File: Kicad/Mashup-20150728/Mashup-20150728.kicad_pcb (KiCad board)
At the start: 2 copper layers, 99.1 x 88.9 mm, 132 parts, among them P1 TST, P10 SPADE_187, P2 CONN_4, P3 CONN_4, P4 CONN2X3MOLEX, P4 CONN_4, P4 CONN_6, P4 SPADE_187, P5 CONN_4, P5 CONN_4X2, P5 CONN_8, P6 CONN_2, P6 CONN_4, P6 CONN_4X2, P6 CONN_8, P7 CONN_4, P7 CONN_8, Q1 MOSFET_N, Q2 MOSFET_N, Q3 MOSFET_N, Q4 MOSFET_N, Q5 MOSFET_N, Q6 MOSFET_N, Q7 MOSFET_N, Q8 MOSFET_N

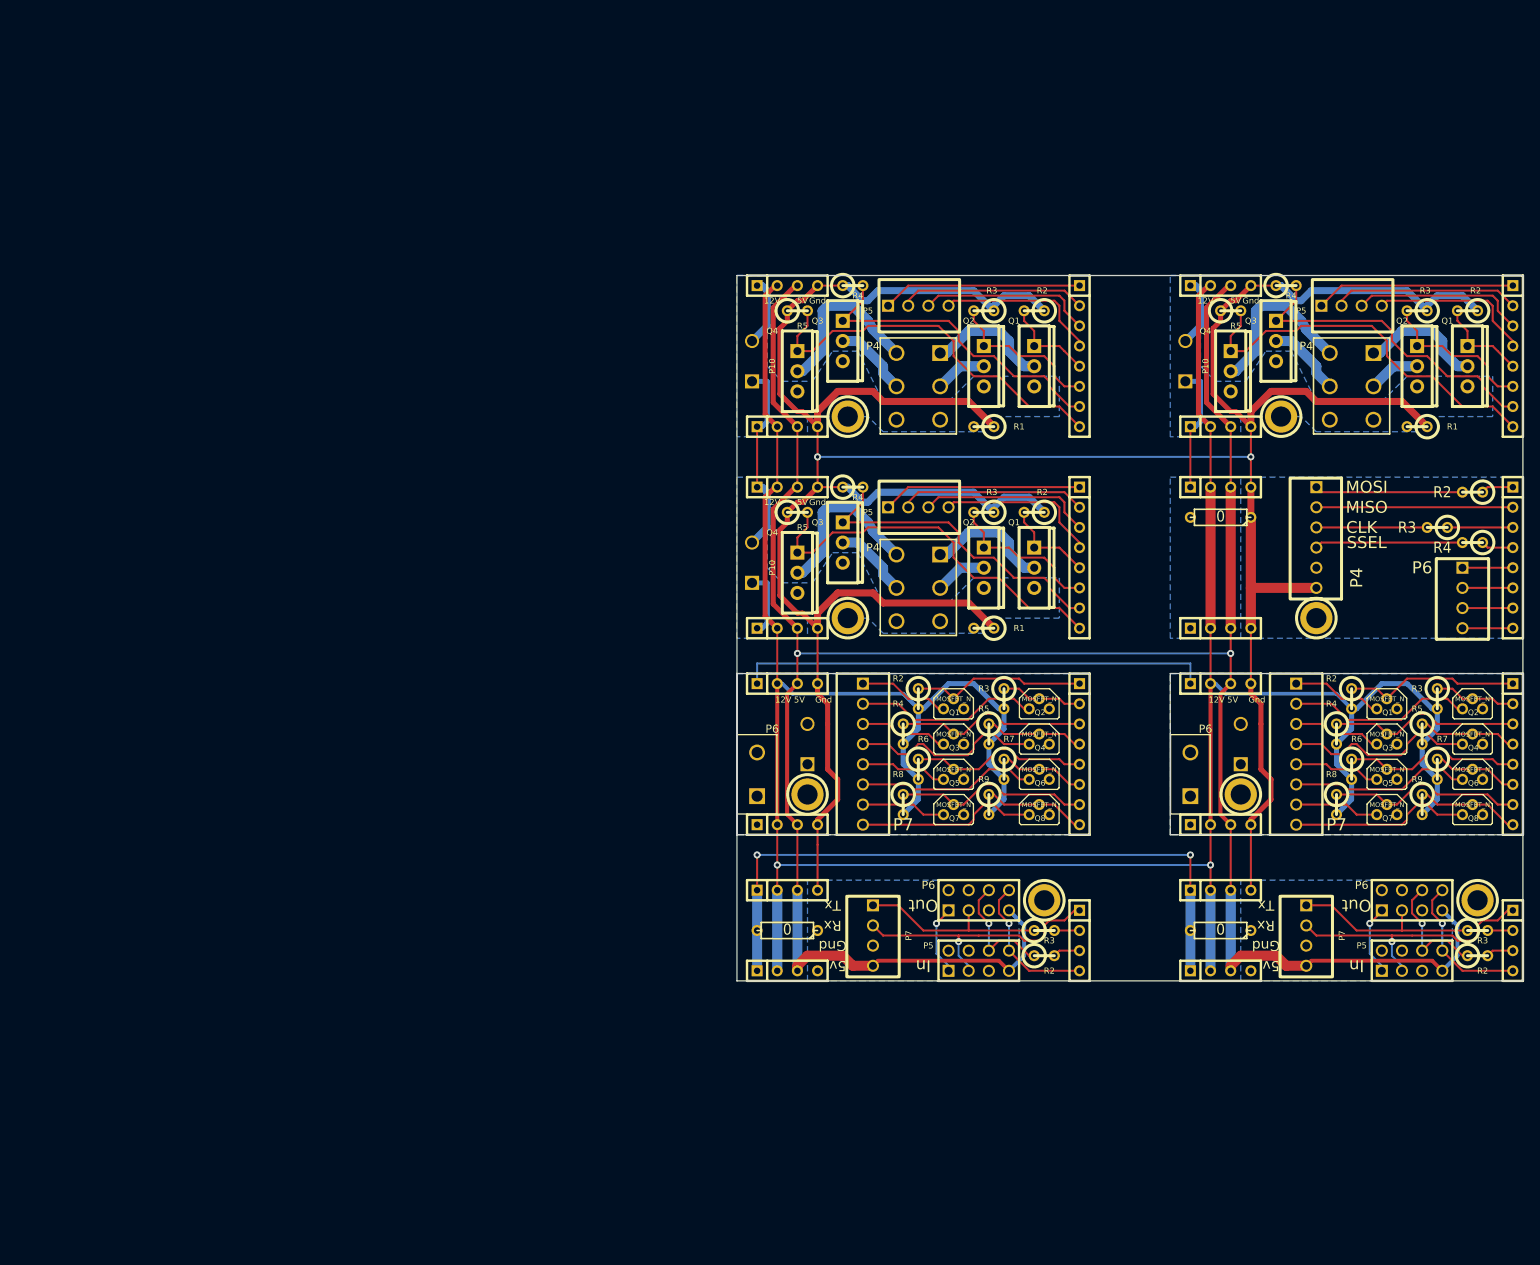
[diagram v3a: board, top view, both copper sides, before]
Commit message: Changed size of PCB sheets to 8.5" x 11".  Added name/rev/board name to PCB sheets.
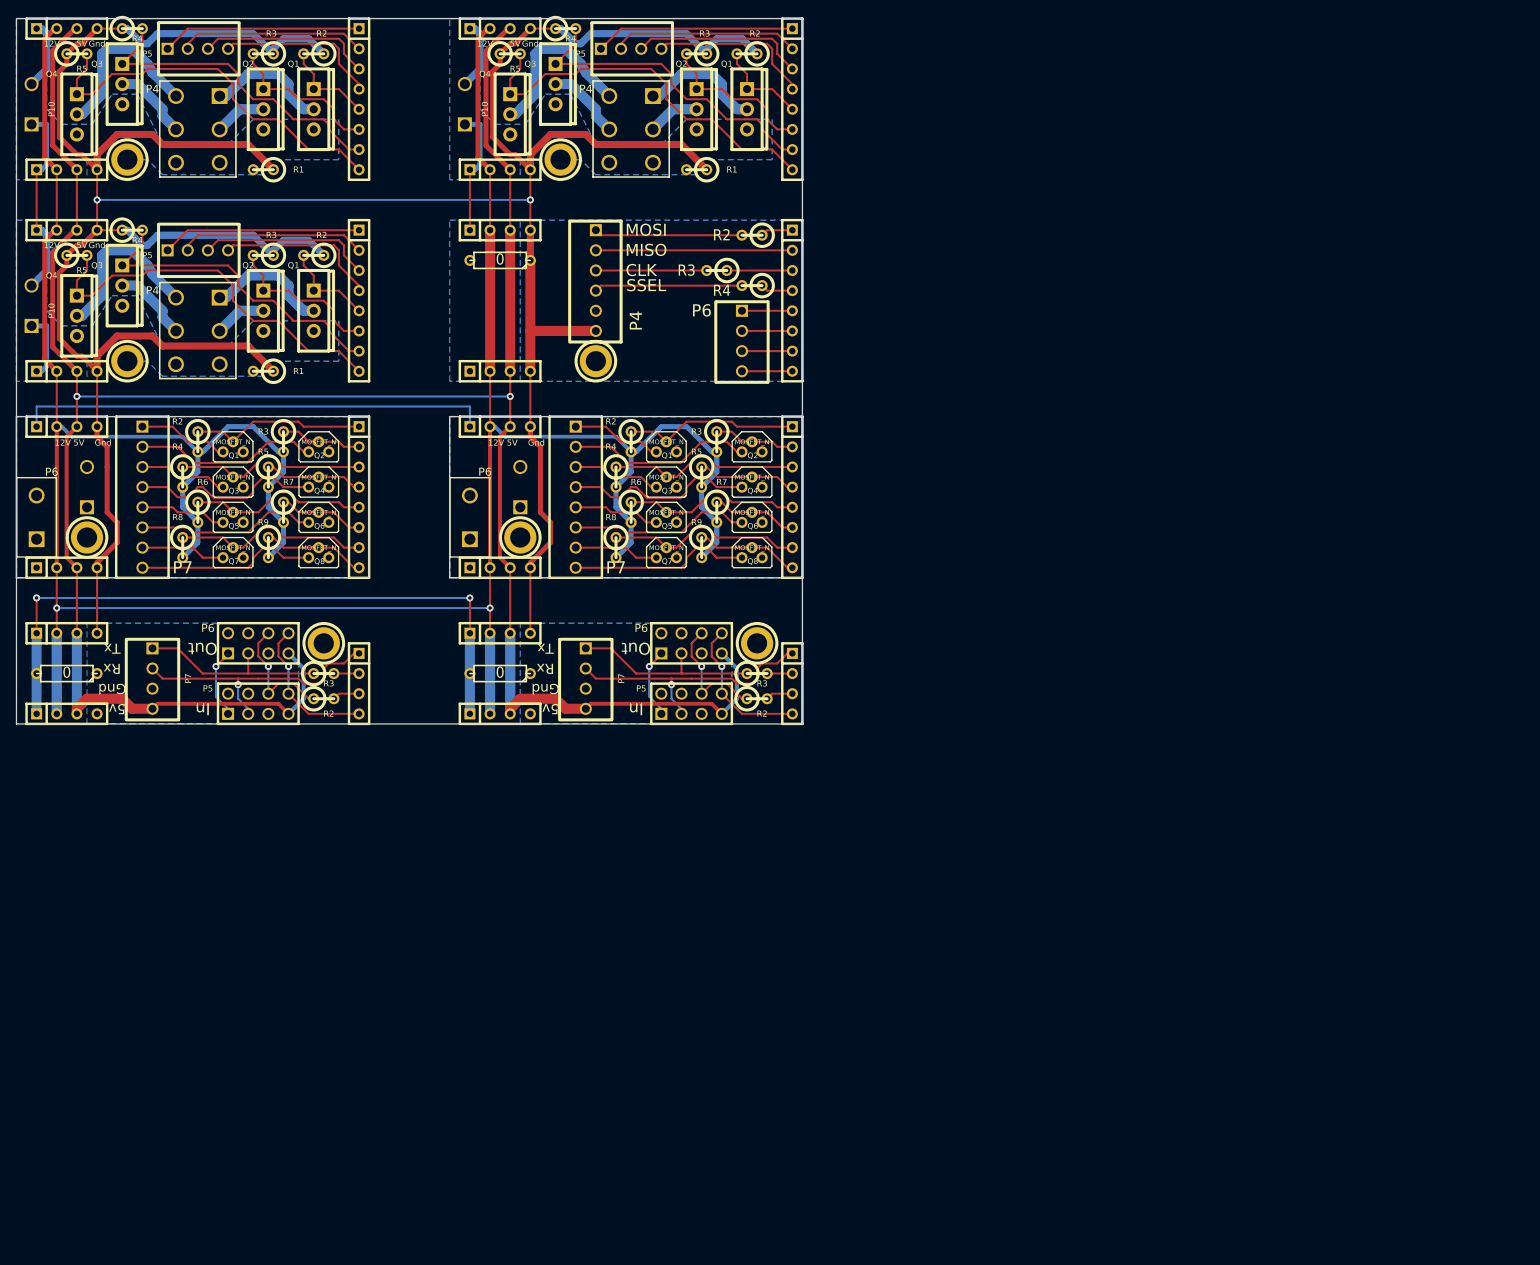
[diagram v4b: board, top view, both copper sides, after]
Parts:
- removed the P1 at (139.7, 106.7)
- removed the P1 at (194.3, 81.3)
- removed the P1 at (139.7, 81.3)
- removed the P1 at (219.1, 142.2)
- removed the P1 at (164.5, 142.2)
- removed the P1 at (134.6, 128.9)
- removed the P1 at (189.2, 128.9)
- removed the P10 at (182.2, 74.3)
- removed the P10 at (127.6, 99.7)
- removed the P10 at (127.6, 74.3)
- removed the P2 at (186.7, 64.8)
- removed the P2 at (132.1, 90.2)
- removed the P2 at (132.1, 64.8)
- removed the P2 at (186.7, 151.1)
- removed the P2 at (132.1, 151.1)
- removed the P2 at (132.1, 114.9)
- removed the P2 at (186.7, 114.9)
- removed the P3 at (186.7, 82.5)
- removed the P3 at (132.1, 108.0)
- removed the P3 at (132.1, 82.5)
- removed the P3 at (186.7, 141.0)
- removed the P3 at (132.1, 141.0)
- removed the P3 at (132.1, 132.7)
- removed the P3 at (186.7, 132.7)
- removed the P4 at (203.2, 77.5)
- removed the P4 at (148.6, 102.9)
- removed the P4 at (148.6, 77.5)
- removed the P4 at (223.5, 147.3)
- removed the P4 at (168.9, 147.3)
- removed the P4 at (134.6, 122.6)
- removed the P4 at (189.2, 122.6)
- removed the P5 at (203.2, 67.3)
- removed the P5 at (148.6, 92.7)
- removed the P5 at (148.6, 67.3)
- removed the P5 at (210.8, 149.9)
- removed the P5 at (156.2, 149.9)
- removed the P5 at (168.9, 123.8)
- removed the P5 at (223.5, 123.8)
- removed the P6 at (223.5, 73.7)
- removed the P6 at (168.9, 99.1)
- removed the P6 at (168.9, 73.7)
- removed the P6 at (210.8, 142.2)
- removed the P6 at (156.2, 142.2)
- removed the P6 at (128.3, 126.4)
- removed the P6 at (182.9, 126.4)
- removed the P7 at (197.5, 146.7)
- removed the P7 at (142.9, 146.7)
- removed the P7 at (141.6, 123.8)
- removed the P7 at (196.2, 123.8)
- removed the Q1 at (217.8, 74.9)
- removed the Q1 at (163.2, 100.3)
- removed the Q1 at (163.2, 74.9)
- removed the Q1 at (153.0, 117.5)
- removed the Q1 at (207.6, 117.5)
- removed the Q2 at (211.5, 74.9)
- removed the Q2 at (156.8, 100.3)
- removed the Q2 at (156.8, 74.9)
- removed the Q2 at (163.8, 117.5)
- removed the Q2 at (218.4, 117.5)
- removed the Q3 at (193.7, 71.8)
- removed the Q3 at (139.1, 97.2)
- removed the Q3 at (139.1, 71.8)
- removed the Q3 at (153.0, 121.9)
- removed the Q3 at (207.6, 121.9)
- removed the Q4 at (188.0, 75.6)
- removed the Q4 at (133.3, 101.0)
- removed the Q4 at (133.3, 75.6)
- removed the Q4 at (163.8, 121.9)
- removed the Q4 at (218.4, 121.9)
- removed the Q5 at (153.0, 126.4)
- removed the Q5 at (207.6, 126.4)
- removed the Q6 at (163.8, 126.4)
- removed the Q6 at (218.4, 126.4)
- removed the Q7 at (153.0, 130.8)
- removed the Q7 at (207.6, 130.8)
- removed the Q8 at (163.8, 130.8)
- removed the Q8 at (218.4, 130.8)
- removed the R1 at (211.5, 82.5)
- removed the R1 at (156.8, 108.0)
- removed the R1 at (156.8, 82.5)
- removed the R1 at (186.7, 146.1)
- removed the R1 at (132.1, 146.1)
- removed the R2 at (217.8, 67.9)
- removed the R2 at (163.2, 93.3)
- removed the R2 at (163.2, 67.9)
- removed the R2 at (219.1, 149.2)
- removed the R2 at (164.5, 149.2)
- removed the R2 at (148.6, 116.8)
- removed the R2 at (203.2, 116.8)
- removed the R3 at (211.5, 67.9)
- removed the R3 at (156.8, 93.3)
- removed the R3 at (156.8, 67.9)
- removed the R3 at (219.1, 146.1)
- removed the R3 at (164.5, 146.1)
- removed the R3 at (159.4, 116.8)
- removed the R3 at (214.0, 116.8)
- removed the R4 at (194.9, 64.8)
- removed the R4 at (140.3, 90.2)
- removed the R4 at (140.3, 64.8)
- removed the R4 at (146.7, 121.3)
- removed the R4 at (201.3, 121.3)
- removed the R5 at (188.0, 67.9)
- removed the R5 at (133.3, 93.3)
- removed the R5 at (133.3, 67.9)
- removed the R5 at (157.5, 121.3)
- removed the R5 at (212.1, 121.3)
- removed the R6 at (148.6, 125.7)
- removed the R6 at (203.2, 125.7)
- removed the R7 at (159.4, 125.7)
- removed the R7 at (214.0, 125.7)
- removed the R8 at (146.7, 130.2)
- removed the R8 at (201.3, 130.2)
- removed the R9 at (157.5, 130.2)
- removed the R9 at (212.1, 130.2)
- removed the VAL at (138.4, 122.6)
- removed the VAL at (193.0, 122.6)
- added P1: TST, 00_mtg_hole-2-56, F.Cu at (48.9, 74.3)
- added P1: TST, 00_mtg_hole-2-56, F.Cu at (103.5, 48.9)
- added P1: TST, 00_mtg_hole-2-56, F.Cu at (48.9, 48.9)
- added P1: TST, 00_mtg_hole-2-56, F.Cu at (128.3, 109.9)
- added P1: TST, 00_mtg_hole-2-56, F.Cu at (73.7, 109.9)
- added P1: TST, 00_mtg_hole-2-56, F.Cu at (43.8, 96.5)
- added P1: TST, 00_mtg_hole-2-56, F.Cu at (98.4, 96.5)
- added P10: SPADE_187, 00_th1x2x200, F.Cu at (91.4, 41.9)
- added P10: SPADE_187, 00_th1x2x200, F.Cu at (36.8, 67.3)
- added P10: SPADE_187, 00_th1x2x200, F.Cu at (36.8, 41.9)
- added P2: CONN_4, SIL-4, F.Cu at (95.9, 32.4)
- added P2: CONN_4, SIL-4, F.Cu at (41.3, 57.8)
- added P2: CONN_4, SIL-4, F.Cu at (41.3, 32.4)
- added P2: CONN_4, SIL-4, F.Cu at (95.9, 118.7)
- added P2: CONN_4, SIL-4, F.Cu at (41.3, 118.7)
- added P2: CONN_4, SIL-4, F.Cu at (41.3, 82.5)
- added P2: CONN_4, SIL-4, F.Cu at (95.9, 82.5)
- added P3: CONN_4, SIL-4, F.Cu at (95.9, 50.2)
- added P3: CONN_4, SIL-4, F.Cu at (41.3, 75.6)
- added P3: CONN_4, SIL-4, F.Cu at (41.3, 50.2)
- added P3: CONN_4, SIL-4, F.Cu at (95.9, 108.6)
- added P3: CONN_4, SIL-4, F.Cu at (41.3, 108.6)
- added P3: CONN_4, SIL-4, F.Cu at (41.3, 100.3)
- added P3: CONN_4, SIL-4, F.Cu at (95.9, 100.3)
- added P4: CONN2X3MOLEX, 00_th2x3x4.2mm_nopeg, F.Cu at (112.4, 45.1)
- added P4: CONN2X3MOLEX, 00_th2x3x4.2mm_nopeg, F.Cu at (57.8, 70.5)
- added P4: CONN2X3MOLEX, 00_th2x3x4.2mm_nopeg, F.Cu at (57.8, 45.1)
- added P4: CONN_4, SIL-4, F.Cu at (132.7, 114.9)
- added P4: CONN_4, SIL-4, F.Cu at (78.1, 114.9)
- added P4: SPADE_187, 00_th1x2x200, F.Cu at (43.8, 90.2)
- added P4: SPADE_187, 00_th1x2x200, F.Cu at (98.4, 90.2)
- added P5: CONN_4, 00_th1x4x100-lock, F.Cu at (112.4, 34.9)
- added P5: CONN_4, 00_th1x4x100-lock, F.Cu at (57.8, 60.3)
- added P5: CONN_4, 00_th1x4x100-lock, F.Cu at (57.8, 34.9)
- added P5: CONN_4X2, pin_array_4x2, F.Cu at (120.0, 117.5)
- added P5: CONN_4X2, pin_array_4x2, F.Cu at (65.4, 117.5)
- added P5: CONN_8, SIL-8, F.Cu at (78.1, 91.4)
- added P5: CONN_8, SIL-8, F.Cu at (132.7, 91.4)
- added P6: CONN_8, SIL-8, F.Cu at (132.7, 41.3)
- added P6: CONN_8, SIL-8, F.Cu at (78.1, 66.7)
- added P6: CONN_8, SIL-8, F.Cu at (78.1, 41.3)
- added P6: CONN_4X2, pin_array_4x2, F.Cu at (120.0, 109.9)
- added P6: CONN_4X2, pin_array_4x2, F.Cu at (65.4, 109.9)
- added P6: CONN_2, 00_th1x2x4.2mm_nopeg, F.Cu at (37.5, 94.0)
- added P6: CONN_2, 00_th1x2x4.2mm_nopeg, F.Cu at (92.1, 94.0)
- added P7: CONN_4, 00_th1x4x100-lock, F.Cu at (106.7, 114.3)
- added P7: CONN_4, 00_th1x4x100-lock, F.Cu at (52.1, 114.3)
- added P7: CONN_8, 00_th1x8x100-lock, F.Cu at (50.8, 91.4)
- added P7: CONN_8, 00_th1x8x100-lock, F.Cu at (105.4, 91.4)
- added Q1: MOSFET_N, 00_to220_vert_gds, F.Cu at (127.0, 42.5)
- added Q1: MOSFET_N, 00_to220_vert_gds, F.Cu at (72.4, 67.9)
- added Q1: MOSFET_N, 00_to220_vert_gds, F.Cu at (72.4, 42.5)
- added Q1: MOSFET_N, 00_to92_sgd, F.Cu at (62.2, 85.1)
- added Q1: MOSFET_N, 00_to92_sgd, F.Cu at (116.8, 85.1)
- added Q2: MOSFET_N, 00_to220_vert_gds, F.Cu at (120.7, 42.5)
- added Q2: MOSFET_N, 00_to220_vert_gds, F.Cu at (66.0, 67.9)
- added Q2: MOSFET_N, 00_to220_vert_gds, F.Cu at (66.0, 42.5)
- added Q2: MOSFET_N, 00_to92_sgd, F.Cu at (73.0, 85.1)
- added Q2: MOSFET_N, 00_to92_sgd, F.Cu at (127.6, 85.1)
- added Q3: MOSFET_N, 00_to220_vert_gds, F.Cu at (102.9, 39.4)
- added Q3: MOSFET_N, 00_to220_vert_gds, F.Cu at (48.3, 64.8)
- added Q3: MOSFET_N, 00_to220_vert_gds, F.Cu at (48.3, 39.4)
- added Q3: MOSFET_N, 00_to92_sgd, F.Cu at (62.2, 89.5)
- added Q3: MOSFET_N, 00_to92_sgd, F.Cu at (116.8, 89.5)
- added Q4: MOSFET_N, 00_to220_vert_gds, F.Cu at (97.2, 43.2)
- added Q4: MOSFET_N, 00_to220_vert_gds, F.Cu at (42.5, 68.6)
- added Q4: MOSFET_N, 00_to220_vert_gds, F.Cu at (42.5, 43.2)
- added Q4: MOSFET_N, 00_to92_sgd, F.Cu at (73.0, 89.5)
- added Q4: MOSFET_N, 00_to92_sgd, F.Cu at (127.6, 89.5)
- added Q5: MOSFET_N, 00_to92_sgd, F.Cu at (62.2, 94.0)
- added Q5: MOSFET_N, 00_to92_sgd, F.Cu at (116.8, 94.0)
- added Q6: MOSFET_N, 00_to92_sgd, F.Cu at (73.0, 94.0)
- added Q6: MOSFET_N, 00_to92_sgd, F.Cu at (127.6, 94.0)
- added Q7: MOSFET_N, 00_to92_sgd, F.Cu at (62.2, 98.4)
- added Q7: MOSFET_N, 00_to92_sgd, F.Cu at (116.8, 98.4)
- added Q8: MOSFET_N, 00_to92_sgd, F.Cu at (73.0, 98.4)
- added Q8: MOSFET_N, 00_to92_sgd, F.Cu at (127.6, 98.4)
- added R1: 100K, R1, F.Cu at (120.7, 50.2)
- added R1: 100K, R1, F.Cu at (66.0, 75.6)
- added R1: 100K, R1, F.Cu at (66.0, 50.2)
- added R1: 0, R3, F.Cu at (95.9, 113.7)
- added R1: 0, R3, F.Cu at (41.3, 113.7)
- added R2: 100K, R1, F.Cu at (127.0, 35.6)
- added R2: 100K, R1, F.Cu at (72.4, 61.0)
- added R2: 100K, R1, F.Cu at (72.4, 35.6)
- added R2: 480, R1, F.Cu at (128.3, 116.8)
- added R2: 480, R1, F.Cu at (73.7, 116.8)
- added R2: 10K, R1, F.Cu at (57.8, 84.5)
- added R2: 10K, R1, F.Cu at (112.4, 84.5)
- added R3: 100K, R1, F.Cu at (120.7, 35.6)
- added R3: 100K, R1, F.Cu at (66.0, 61.0)
- added R3: 100K, R1, F.Cu at (66.0, 35.6)
- added R3: 480, R1, F.Cu at (128.3, 113.7)
- added R3: 480, R1, F.Cu at (73.7, 113.7)
- added R3: 10K, R1, F.Cu at (68.6, 84.5)
- added R3: 10K, R1, F.Cu at (123.2, 84.5)
- added R4: 100K, R1, F.Cu at (104.1, 32.4)
- added R4: 100K, R1, F.Cu at (49.5, 57.8)
- added R4: 100K, R1, F.Cu at (49.5, 32.4)
- added R4: 10K, R1, F.Cu at (55.9, 88.9)
- added R4: 10K, R1, F.Cu at (110.5, 88.9)
- added R5: 0, R1, F.Cu at (97.2, 35.6)
- added R5: 0, R1, F.Cu at (42.5, 61.0)
- added R5: 0, R1, F.Cu at (42.5, 35.6)
- added R5: 10K, R1, F.Cu at (66.7, 88.9)
- added R5: 10K, R1, F.Cu at (121.3, 88.9)
- added R6: 10K, R1, F.Cu at (57.8, 93.3)
- added R6: 10K, R1, F.Cu at (112.4, 93.3)
- added R7: 10K, R1, F.Cu at (68.6, 93.3)
- added R7: 10K, R1, F.Cu at (123.2, 93.3)
- added R8: 10K, R1, F.Cu at (55.9, 97.8)
- added R8: 10K, R1, F.Cu at (110.5, 97.8)
- added R9: 10K, R1, F.Cu at (66.7, 97.8)
- added R9: 10K, R1, F.Cu at (121.3, 97.8)
- added VAL: REF, opp_logo_backsilk, F.Cu at (47.6, 90.2)
- added VAL: REF, opp_logo_backsilk, F.Cu at (102.2, 90.2)
- moved P5 96.4 mm to (132.7, 66.7)
- moved R3 96.4 mm to (123.2, 62.9)
- moved VAL 96.4 mm to (127.0, 48.9)
- moved VAL 96.4 mm to (117.5, 73.7)
- moved P1 96.4 mm to (108.0, 74.3)
- moved P2 96.4 mm to (95.9, 75.6)
- moved P3 96.4 mm to (95.9, 57.8)
- moved P4 96.4 mm to (108.0, 64.1)
- moved P6 96.4 mm to (126.4, 71.8)
- moved R1 96.4 mm to (95.9, 61.6)
- moved R2 96.4 mm to (127.6, 58.4)
- moved R4 96.4 mm to (127.6, 64.8)
- moved VAL 96.4 mm to (72.4, 48.9)
- moved VAL 96.4 mm to (72.4, 74.3)
- moved VAL 96.4 mm to (56.5, 114.3)
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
